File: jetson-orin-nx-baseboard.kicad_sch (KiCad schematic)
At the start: 0 parts

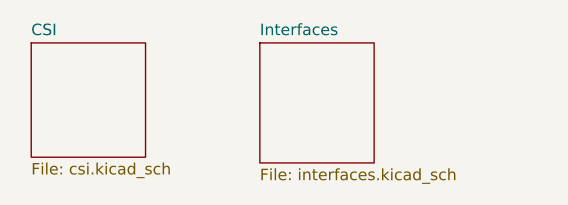
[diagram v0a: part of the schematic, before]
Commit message: Connected gpio signals and 40-pin connector
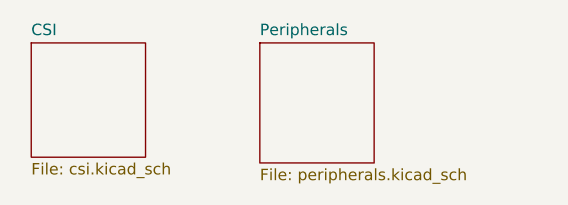
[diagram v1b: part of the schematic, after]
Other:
- sheet Interfaces renamed Peripherals
- sheet Peripherals: file interfaces.kicad_sch -> peripherals.kicad_sch

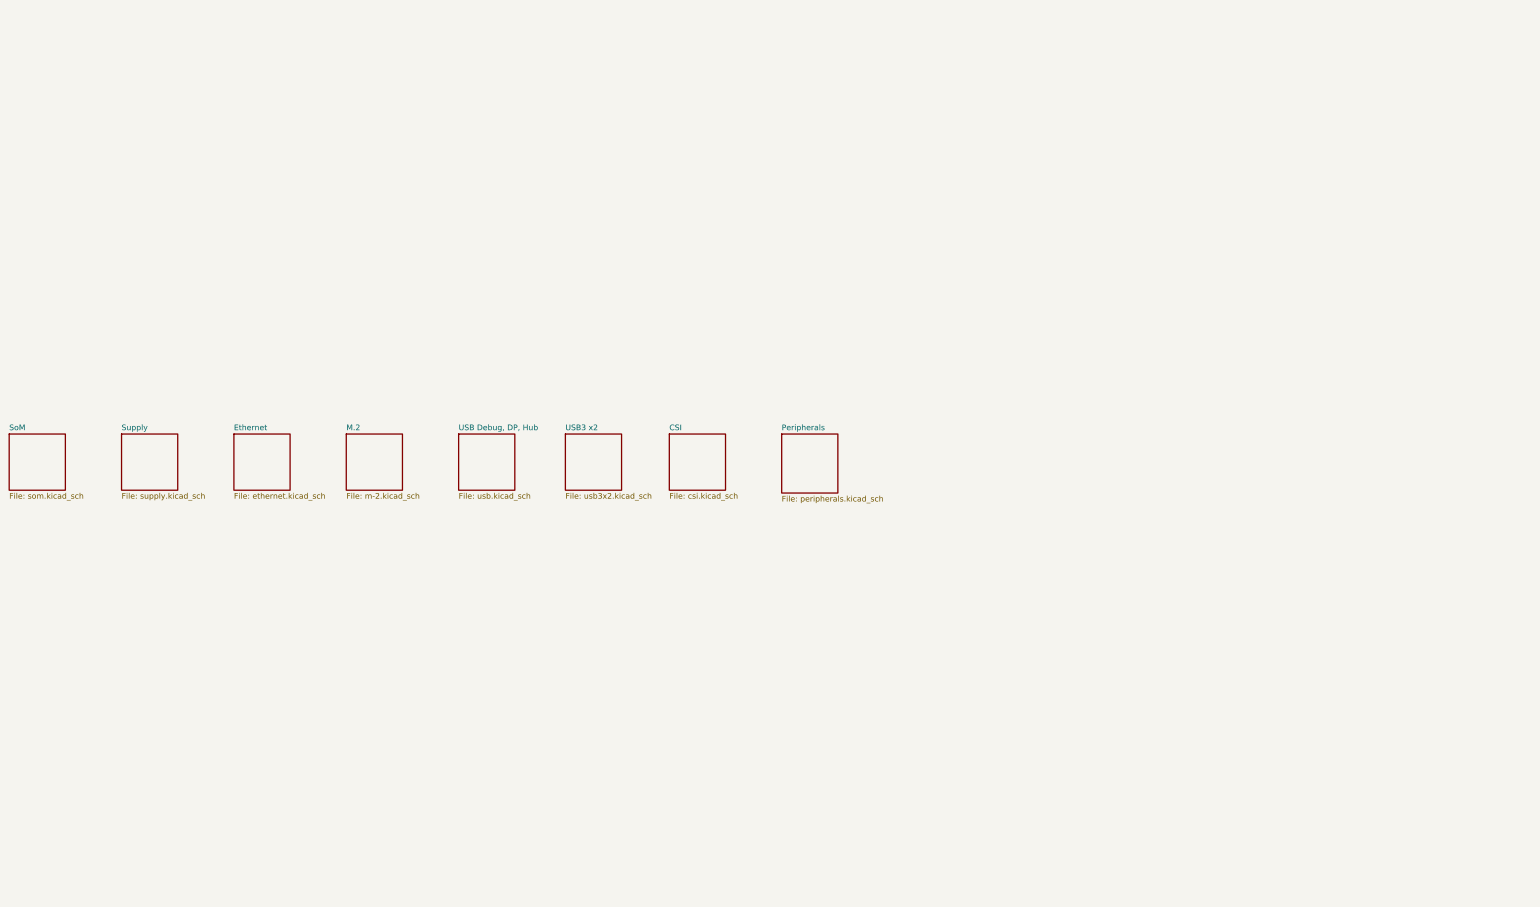
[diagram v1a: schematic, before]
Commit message: Cleaned up schematics, added debug connector, user LEDs and buttons. Connected misc. signals
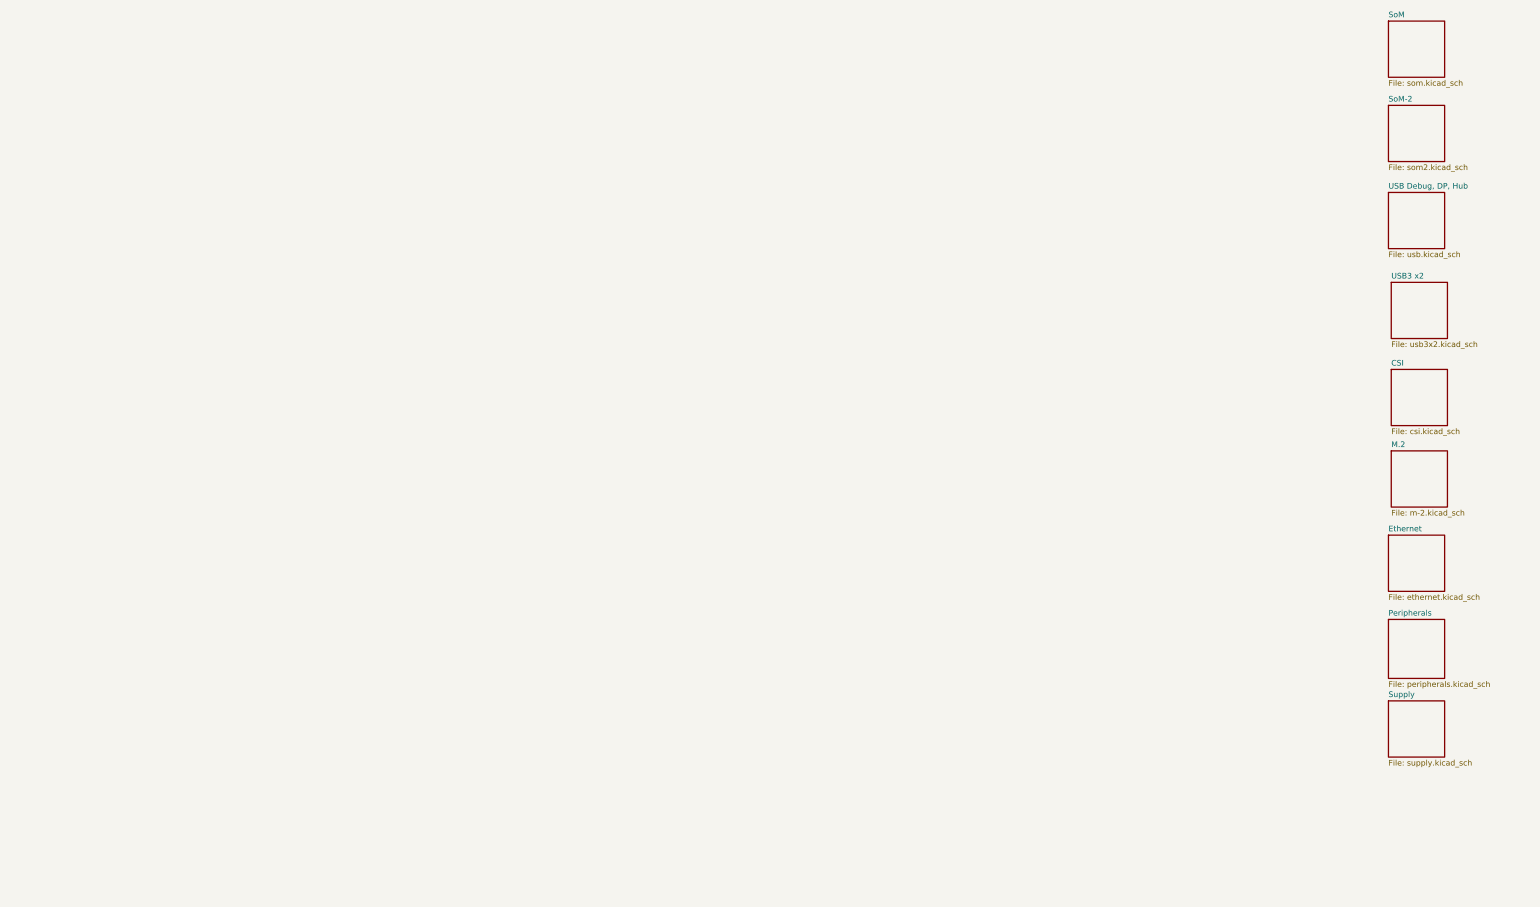
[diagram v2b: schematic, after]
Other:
- added sheet SoM-2 (som2.kicad_sch)

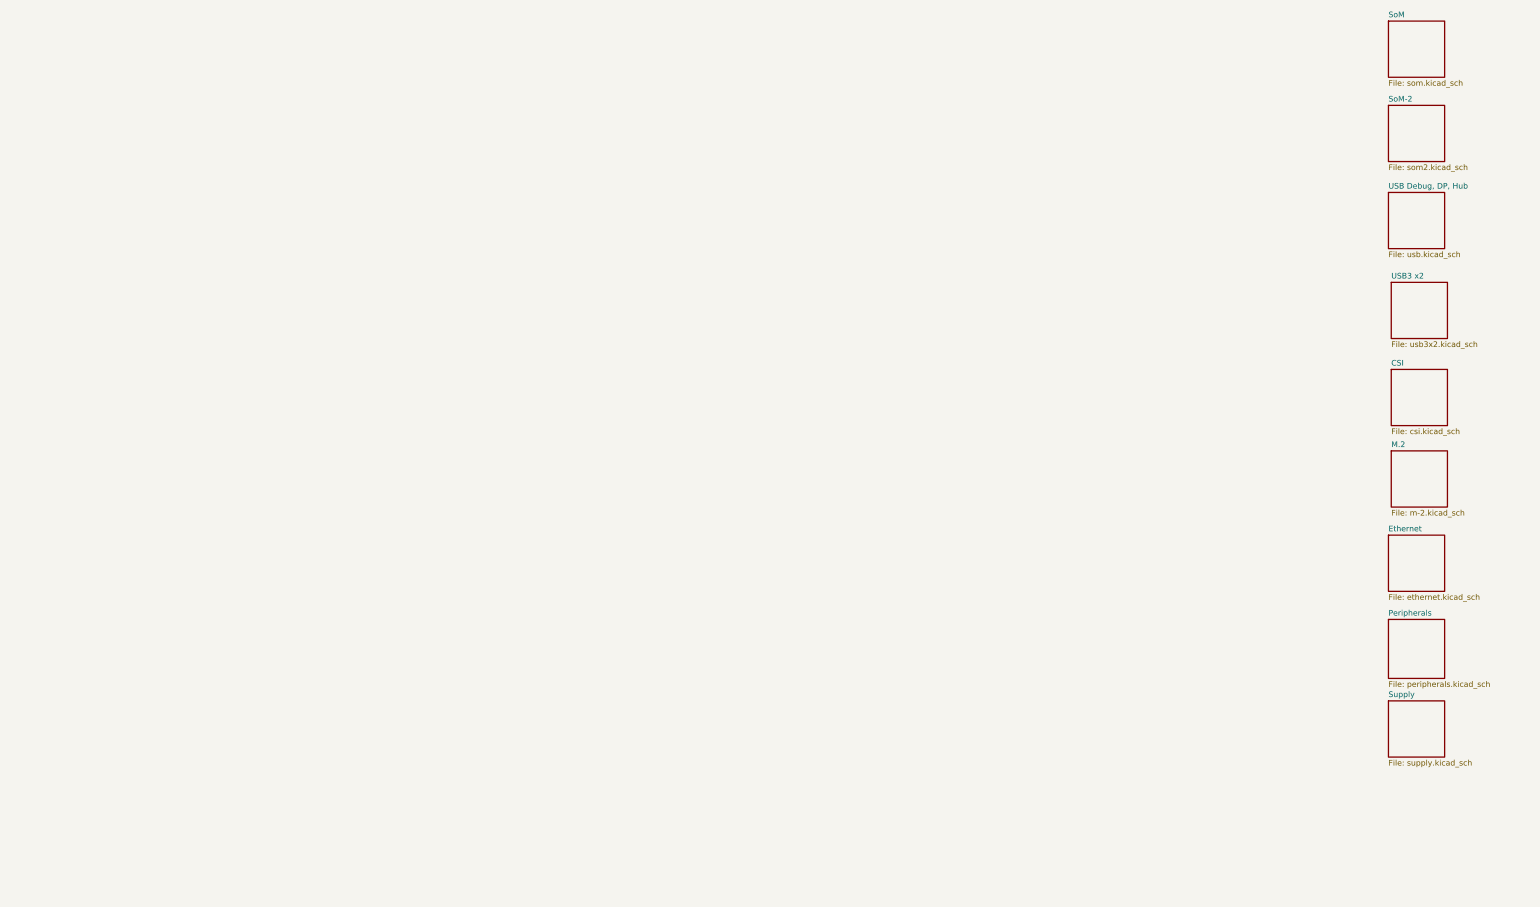
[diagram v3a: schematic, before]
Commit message: Remove SoM2 subsheet
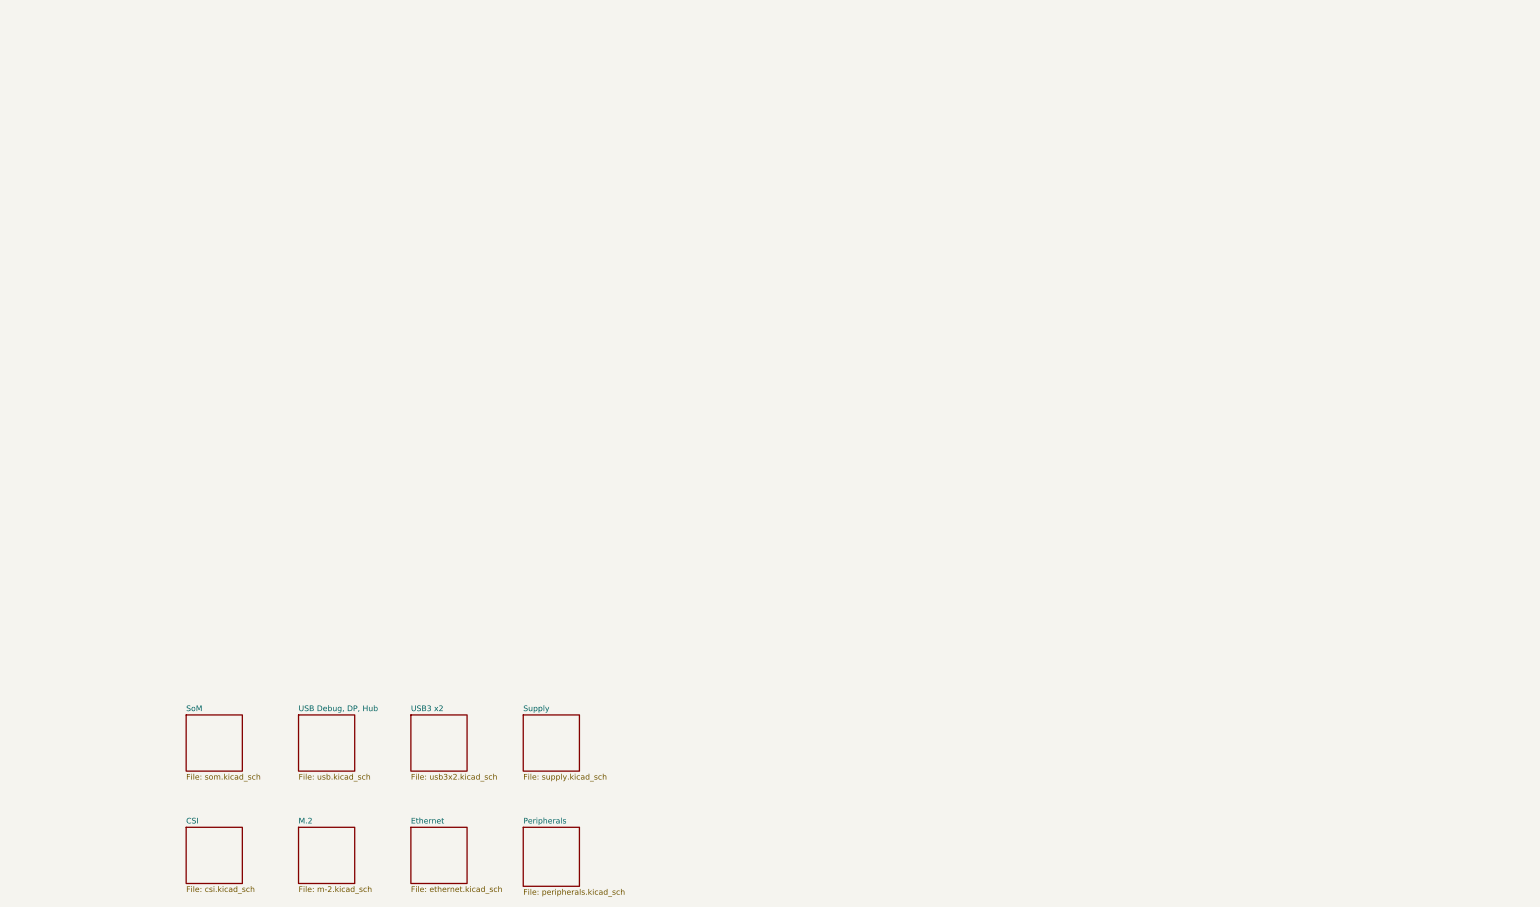
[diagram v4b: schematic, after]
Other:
- removed sheet SoM-2
